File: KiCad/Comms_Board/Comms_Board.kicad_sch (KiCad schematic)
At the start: 5 parts, among them J1 Screw_Terminal_01x02, J2 Screw_Terminal_01x02, J3 Screw_Terminal_01x02

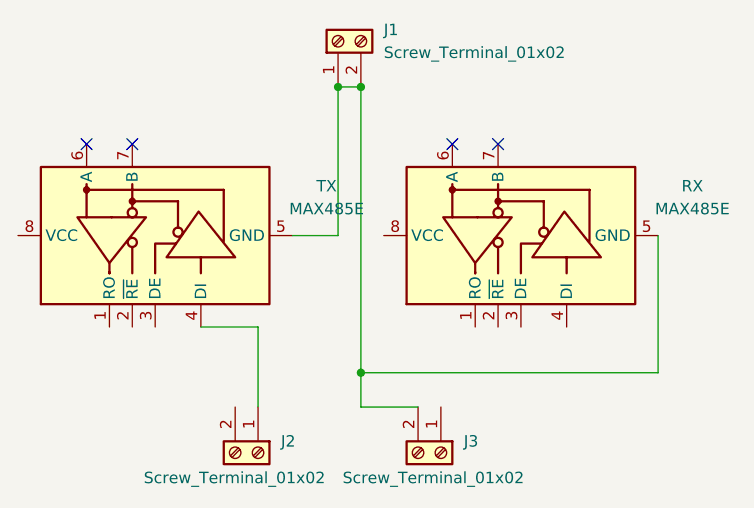
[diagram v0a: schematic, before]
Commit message: Communications board for RS485
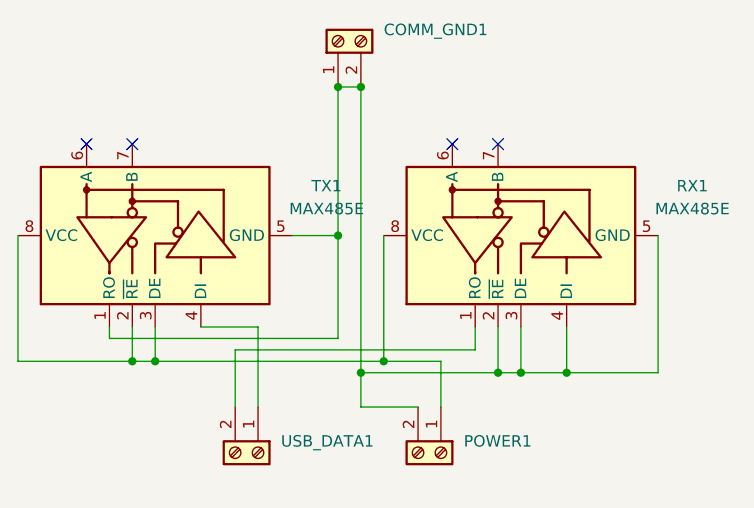
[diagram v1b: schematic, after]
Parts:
- COMM_GND1: renamed from J1; footprint (none) -> TerminalBlock:TerminalBlock_bornier-2_P5.08mm
- POWER1: renamed from J3; footprint (none) -> TerminalBlock:TerminalBlock_bornier-2_P5.08mm
- RX1: renamed from RX; footprint Package_SO:SOIC-8_3.9x4.9mm_P1.27mm -> Communications:RS485_Transceiver
- TX1: renamed from TX; footprint Package_SO:SOIC-8_3.9x4.9mm_P1.27mm -> Communications:RS485_Transceiver
- USB_DATA1: renamed from J2; footprint (none) -> TerminalBlock:TerminalBlock_bornier-2_P5.08mm
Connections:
- net at TX1.1 (RO): now also COMM_GND1.1 (Pin_1), COMM_GND1.2 (Pin_2), POWER1.2 (Pin_2), RX1.2 (~{RE}), RX1.3 (DE), RX1.4 (DI), RX1.5 (GND), TX1.5 (GND)
- net at TX1.2 (~{RE}): now also POWER1.1 (Pin_1), RX1.8 (VCC), TX1.3 (DE), TX1.8 (VCC)
- net at USB_DATA1.2 (Pin_2): now also RX1.1 (RO)
